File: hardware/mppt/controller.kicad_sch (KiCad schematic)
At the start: 0 parts

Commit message: run through mppt sch, going through bom
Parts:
- added C201, C205: 6p, symbol Device:C_Small
- added C202, C206: 4.3p, symbol Device:C_Small
- added C203: 10u, symbol Device:C_Small
- added C204, C207, C208, C209, C211, C212, C213: 100n, symbol Device:C_Small
- added C210: 4.7u, symbol Device:C_Small
- added C214: 1u, symbol Device:C_Small
- added D201, D202, D203: RED, symbol Device:LED_Small
- added FB201: FerriteBead, symbol Device:FerriteBead
- added JP201, JP202: Jumper_2_Bridged, Connector_PinHeader_2.54mm:PinHeader_1x02_P2.54mm_Vertical, symbol Jumper:Jumper_2_Bridged
- added R201: 47, symbol Device:R_Small
- added R202: 10k, symbol Device:R_Small
- added R203, R204, R205: 1k, symbol Device:R_Small
- added SW201: SW_SPST, Button_Switch_THT:SW_PUSH_6mm, symbol Switch:SW_SPST
- added TP201, TP202, TP203, TP204, TP205, TP206, TP207, TP208: TestPoint_Small, symbol Connector:TestPoint_Small
- added U201: STM32F446RETx, Package_QFP:LQFP-64_10x10mm_P0.5mm, symbol MCU_ST_STM32F4:STM32F446RETx
- added Y201: 25MHz, Crystal:Crystal_SMD_Abracon_ABM8AIG-4Pin_3.2x2.5mm, symbol Device:Crystal_GND24
- added Y202: 32kHz, Crystal:Crystal_SMD_Abracon_ABS25-4Pin_8.0x3.8mm, symbol Device:Crystal_GND23
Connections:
- new net: D203.2 (A), R205.2
- new net: D202.2 (A), R204.2
- new net: R202.1, U201.60 (BOOT0)
- new net: JP201.1 (A), JP202.2 (B), R202.2
- new net: D201.2 (A), R203.2
- new net: C205.2, R201.2, Y201.3
- new net: C210.1, U201.30 (VCAP_1)
- new net +3V3: C203.1, C207.1, C208.1, C209.1, C211.1, C212.1, FB201.1, JP201.2 (B), U201.1 (VBAT), U201.19 (VDD), U201.32 (VDD), U201.48 (VDD), U201.64 (VDD)
- new net AL_IN_EN: U201.28 (PB2)
- new net AL_OUT_EN: U201.29 (PB10)
- new net BACKLIGHT_PWM: U201.50 (PA15)
- new net CAN_RX: U201.33 (PB12)
- new net CAN_TX: U201.34 (PB13)
- new net CONV_DISABLE: U201.36 (PB15)
- new net CONV_EN: U201.15 (PA1)
- new net CONV_PWM: U201.16 (PA2)
- new net DC: U201.57 (PB5)
- new net FAN_PWM: U201.14 (PA0)
- new net GND: C201.1, C202.1, C203.2, C204.1, C205.1, C206.1, C207.2, C208.2, C209.2, C210.2, C211.2, C212.2, C213.2, C214.2, D201.1 (K), D202.1 (K), D203.1 (K), JP202.1 (A), SW201.1 (A), U201.12 (VSSA), U201.18 (VSS), U201.31 (VSS), U201.47 (VSS), U201.63 (VSS), Y201.2, Y201.4
- new net HSE_IN: C201.2, U201.5 (PH0), Y201.1
- new net HSE_OUT: R201.1, U201.6 (PH1)
- new net LCD_CS: U201.54 (PD2)
- new net LCD_SPI_CIPO: U201.52 (PC11)
- new net LCD_SPI_CLK: U201.51 (PC10)
- new net LCD_SPI_COPI: U201.53 (PC12)
- new net LED1: R203.1, U201.37 (PC6)
- new net LED2: R204.1, U201.38 (PC7)
- new net LED3: R205.1, U201.39 (PC8)
- new net LSE_IN: C202.2, U201.3 (PC14), Y202.1
- new net LSE_OUT: C206.2, U201.4 (PC15), Y202.4
- new net LS_IN_EN: U201.26 (PB0)
- new net LS_OUT_EN: U201.27 (PB1)
- new net MON_ALERT: U201.24 (PC4)
- new net MON_IN_CS: U201.20 (PA4)
- new net MON_OUT_CS: U201.25 (PC5)
- new net MON_SPI_CIPO: U201.22 (PA6)
- new net MON_SPI_CLK: U201.21 (PA5)
- new net MON_SPI_COPI: U201.23 (PA7)
- new net NRST: C204.2, SW201.2 (B), U201.7 (NRST)
- new net PROT_DISABLE: U201.35 (PB14)
- new net RESERVED0: TP201.1, U201.2 (PC13)
- new net RESERVED1: TP202.1, U201.17 (PA3)
- new net RESERVED2: TP203.1, U201.61 (PB8)
- new net RESERVED3: TP204.1, U201.62 (PB9)
- new net RESERVED4: TP205.1, U201.40 (PC9)
- new net RESERVED5: TP206.1, U201.41 (PA8)
- new net RESERVED6: TP207.1, U201.58 (PB6)
- new net RESERVED7: TP208.1, U201.59 (PB7)
- new net RESET: U201.56 (PB4)
- new net SDC_CS: U201.55 (PB3)
- new net SWCLK: U201.49 (PA14)
- new net SWDIO: U201.46 (PA13)
- new net TEMP_BOARD: U201.11 (PC3)
- new net TEMP_HS_FET: U201.10 (PC2)
- new net TEMP_IND: U201.8 (PC0)
- new net TEMP_LS_FET: U201.9 (PC1)
- new net USART_RX: U201.43 (PA10)
- new net USART_TX: U201.42 (PA9)
- new net USB_DM: U201.44 (PA11)
- new net USB_DP: U201.45 (PA12)
- new net VDDA: C213.1, C214.1, FB201.2, U201.13 (VDDA)
- no-connect marks 0 -> 2
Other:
- note added: "Arbitrary. Needs backing math to approve."
- note added: "Assume stray capacitance is 5pF; derive C_{L1|L2} from sec. 3.3 in STM AN2867."
- note added: "Per V_{DD}"
- note added: "To hit 180 MHZ F_{IO}, need 10 pF C_{L}"
- note added: "V_{BAT}"
- title: Mighty MPPT -> Controller

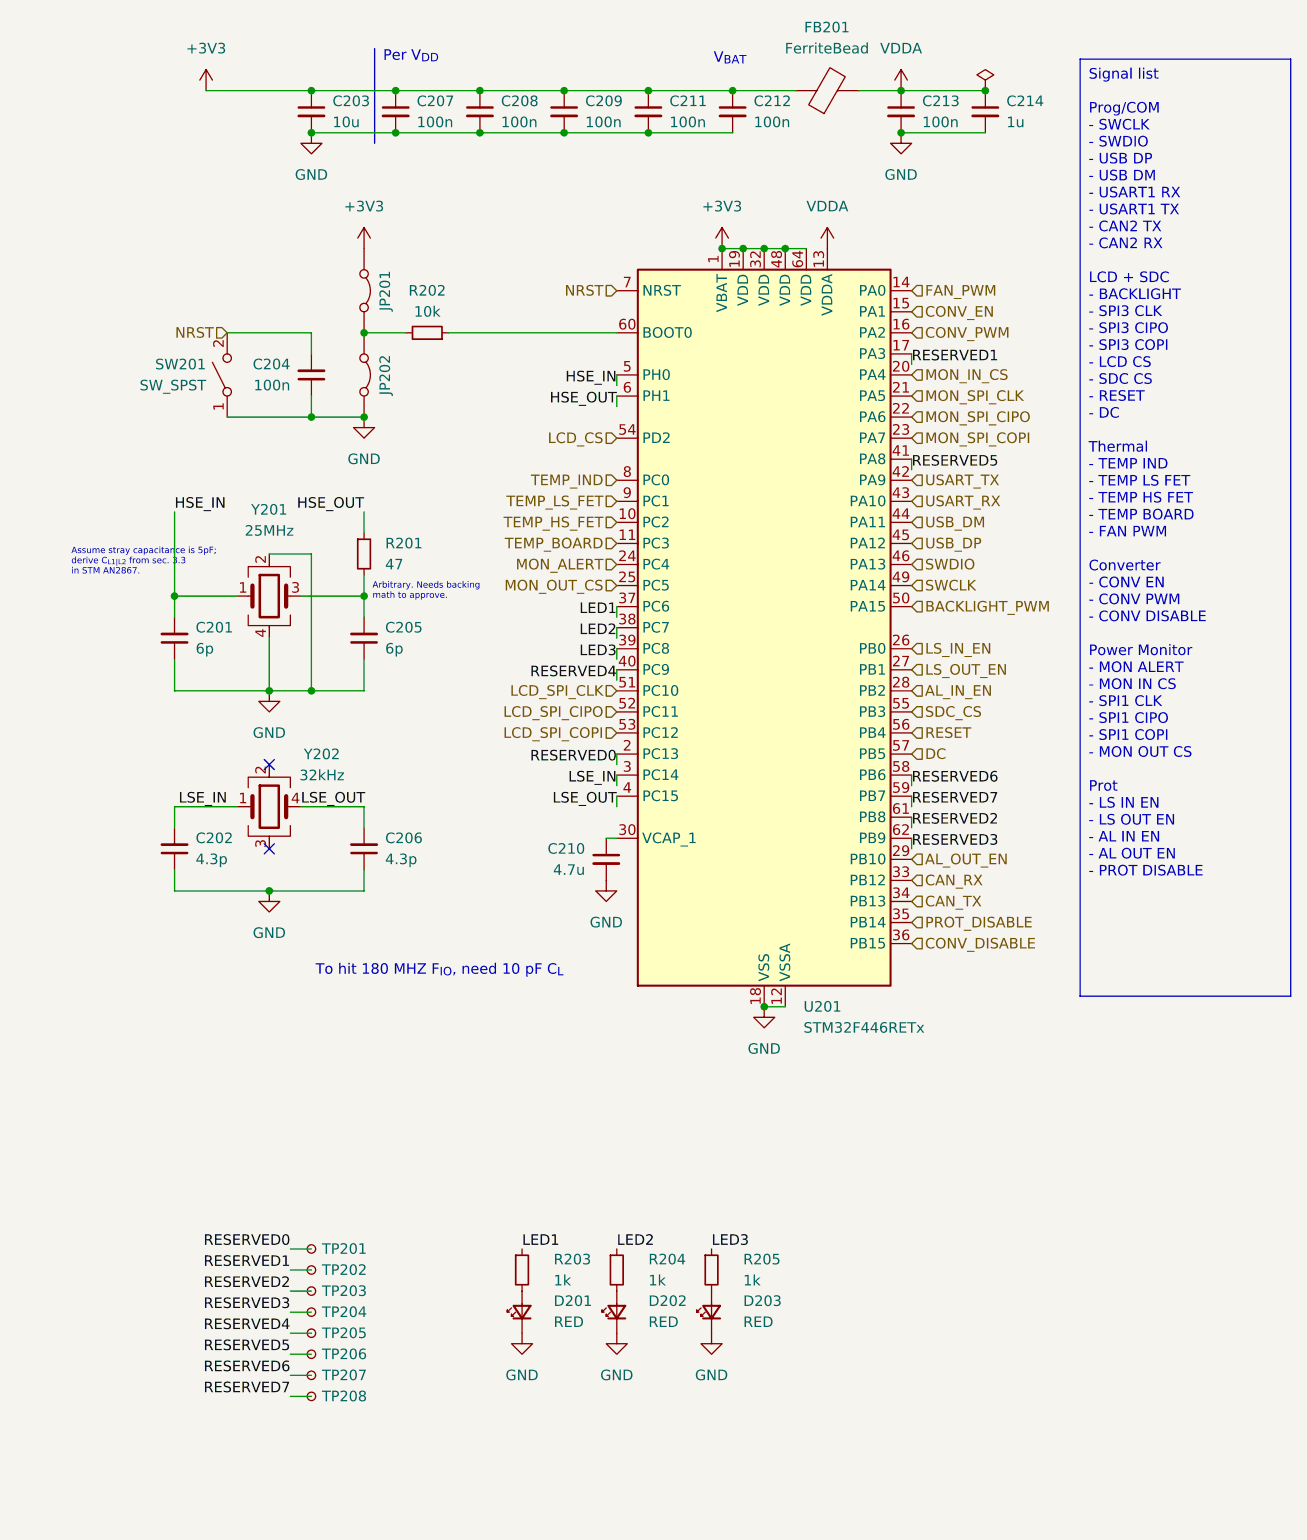
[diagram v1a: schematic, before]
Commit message: update final missing pieces for sch, moving to bom pop
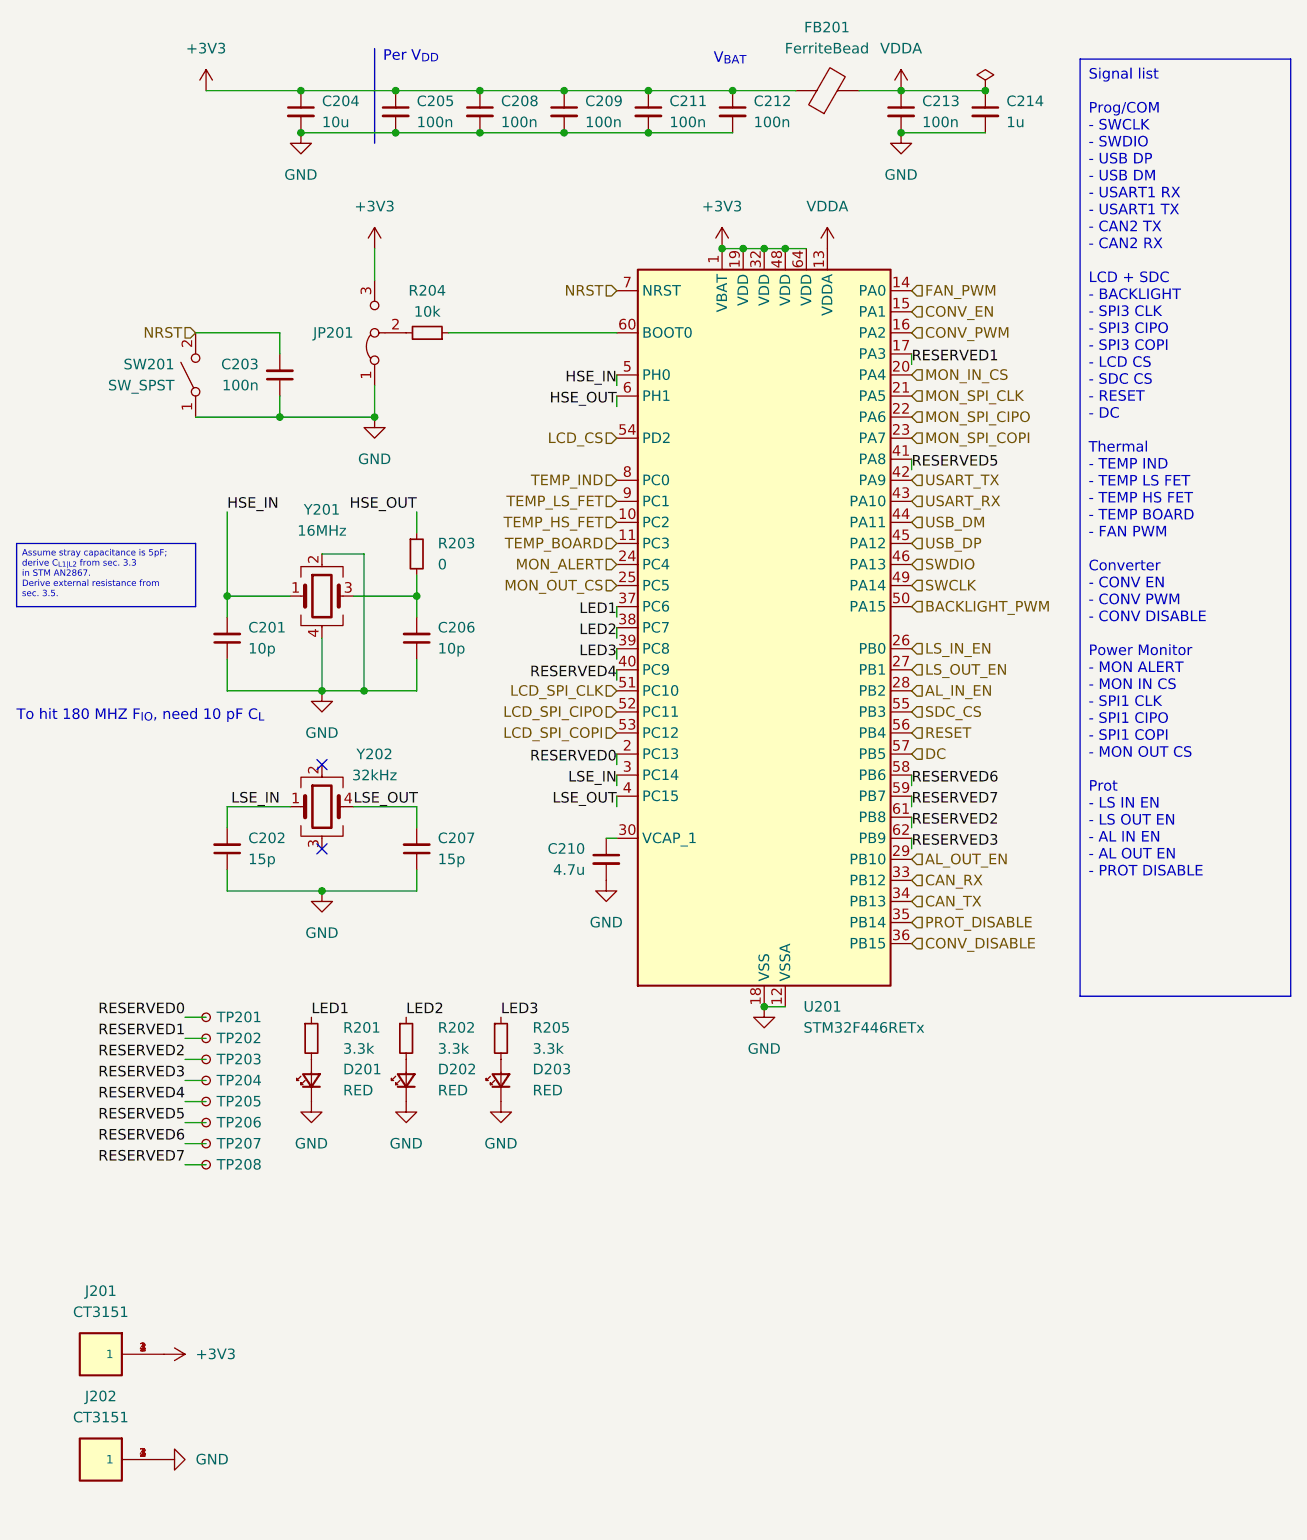
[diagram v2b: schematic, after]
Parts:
- removed C205: 6p, symbol Device:C_Small
- removed JP201, JP202: Jumper_2_Bridged, Connector_PinHeader_2.54mm:PinHeader_1x02_P2.54mm_Vertical, symbol Jumper:Jumper_2_Bridged
- added C207: 15p, symbol Device:C_Small
- added J201, J202: CT3151, footprints:caltest_ct3151, symbol caltest_ct3151:CT3151
- added JP201: Jumper_3_Bridged12, Connector_PinSocket_2.54mm:PinSocket_1x03_P2.54mm_Vertical, symbol Jumper:Jumper_3_Bridged12
- C201: value 6p -> 10p
- C202: value 4.3p -> 15p
- C206: value 4.3p -> 10p
- D201, D202, D203: footprint (none) -> LED_SMD:LED_0805_2012Metric_Pad1.15x1.40mm_HandSolder
- R201: renamed from R203; value 1k -> 3.3k; Manufacturer (none) -> Vishay / Dale
- R202: renamed from R204; value 1k -> 3.3k; Manufacturer (none) -> Vishay / Dale
- R203: renamed from R201; value 47 -> 0; Manufacturer (none) -> Vishay / Dale
- R204: renamed from R202; Manufacturer (none) -> Vishay / Dale
- R205: value 1k -> 3.3k; Manufacturer (none) -> Vishay / Dale
- TP201, TP202, TP203, TP204, TP205, TP206, TP207, TP208: footprint (none) -> TestPoint:TestPoint_Pad_D1.0mm
- U201: Distributor = -> (none)
- Y201: value 25MHz -> 16MHz; footprint Crystal:Crystal_SMD_Abracon_ABM8AIG-4Pin_3.2x2.5mm -> Crystal:Crystal_SMD_Abracon_ABM8G-4Pin_3.2x2.5mm; P/N ABM8AIG-25.000MHZ-8-T -> ABM8G-25.000MHZ-4Y-T3
- Y202: LCSC Part # C1985642 -> (none); P/N ABS25-32.768KHZ-6-T -> ABS25-32.768KHZ-T
- renumbered C204 to C203, C203 to C204, C207 to C205
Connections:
- net +3V3: now also J201.1, J201.2 (1), J201.3 (1), J201.4 (1), JP201.3 (B)
- net GND: now also C207.1, J202.1, J202.2 (1), J202.3 (1), J202.4 (1), JP201.1 (A)
- net LSE_OUT: now also C207.2; no longer C206.2
- net at R204.2: now also JP201.2 (C)
- net at R203.2, Y201.3: now also C206.2
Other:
- note removed: "Arbitrary. Needs backing math to approve."
- note removed: "Assume stray capacitance is 5pF; derive C_{L1|L2} from sec. 3.3 in STM AN2867."
- moved on the sheet: C201, C202, C203, C204, D201, D202, D203, R201, R202, R203, R205, SW201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

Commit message: bom consolidated, starting layout
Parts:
- removed J201, J202: CT3151, footprints:caltest_ct3151, symbol caltest_ct3151:CT3151
- added G201: Jumper, symbol generic_symbol:Generic_Symbol
- added TP201, TP202: TestPoint, TestPoint:TestPoint_Keystone_5000-5004_Miniature, symbol Connector:TestPoint
- C201, C206: footprint (none) -> Capacitor_SMD:C_0402_1005Metric_Pad0.74x0.62mm_HandSolder; Manufacturer Samsung Electro-Mechanics -> TDK; P/N (none) -> CGA2B2C0G1H100D050BA
- C202, C207: footprint (none) -> Capacitor_SMD:C_0402_1005Metric_Pad0.74x0.62mm_HandSolder; Manufacturer Samsung Electro-Mechanics -> TDK; P/N (none) -> CGA2B2C0G1H150J050BA
- C203, C205, C208, C209, C211, C212, C213: footprint (none) -> Capacitor_SMD:C_0402_1005Metric_Pad0.74x0.62mm_HandSolder; Manufacturer Samsung Electro-Mechanics -> TDK; P/N (none) -> CGA2B3X7R1H104K050BB
- C204: footprint (none) -> Capacitor_SMD:C_1206_3216Metric_Pad1.33x1.80mm_HandSolder; Manufacturer Samsung Electro-Mechanics -> TDK; P/N (none) -> CGA5L1X7R1E106K160AC
- C210: footprint (none) -> Capacitor_SMD:C_0805_2012Metric_Pad1.18x1.45mm_HandSolder; Manufacturer Samsung Electro-Mechanics -> TDK; P/N (none) -> CGA4J1X7R1E475K125AC
- C214: footprint (none) -> Capacitor_SMD:C_0603_1608Metric_Pad1.08x0.95mm_HandSolder; Manufacturer Samsung Electro-Mechanics -> TDK; P/N (none) -> CGA3E1X7R1V105K080AC
- D201, D202, D203: Manufacturer (none) -> Kingbright; P/N (none) -> APT2012SURCK
- FB201: footprint (none) -> Resistor_SMD:R_0603_1608Metric_Pad0.98x0.95mm_HandSolder; Manufacturer (none) -> TDK; P/N (none) -> MMZ1608R300ATD25
- R201, R202, R205: footprint (none) -> Resistor_SMD:R_0603_1608Metric_Pad0.98x0.95mm_HandSolder; P/N (none) -> CRCW06033K30FKEA
- R203: footprint (none) -> Resistor_SMD:R_1210_3225Metric_Pad1.30x2.65mm_HandSolder; P/N (none) -> CRCW12100000Z0EA
- R204: footprint (none) -> Resistor_SMD:R_0603_1608Metric_Pad0.98x0.95mm_HandSolder; P/N (none) -> CRCW060310K0FKEA
- SW201: Manufacturer (none) -> CUI Devices; P/N (none) -> TS02-66-150-BK-260-LCR-D
- renumbered TP201 to TP203, TP202 to TP204, TP203 to TP205, TP204 to TP206, TP205 to TP207, TP206 to TP208, TP207 to TP209, TP208 to TP210
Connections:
- net +3V3: now also TP201.1
- net GND: now also TP202.1
